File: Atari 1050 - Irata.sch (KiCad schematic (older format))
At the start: 18 parts, among them J1 6507, J2 Conn_01x05, U1 6502, U2 6264, U3 27C64, U4 74LS42, U5 74LS00, U6 74LS00, U7 74LS139, U8 74LS30

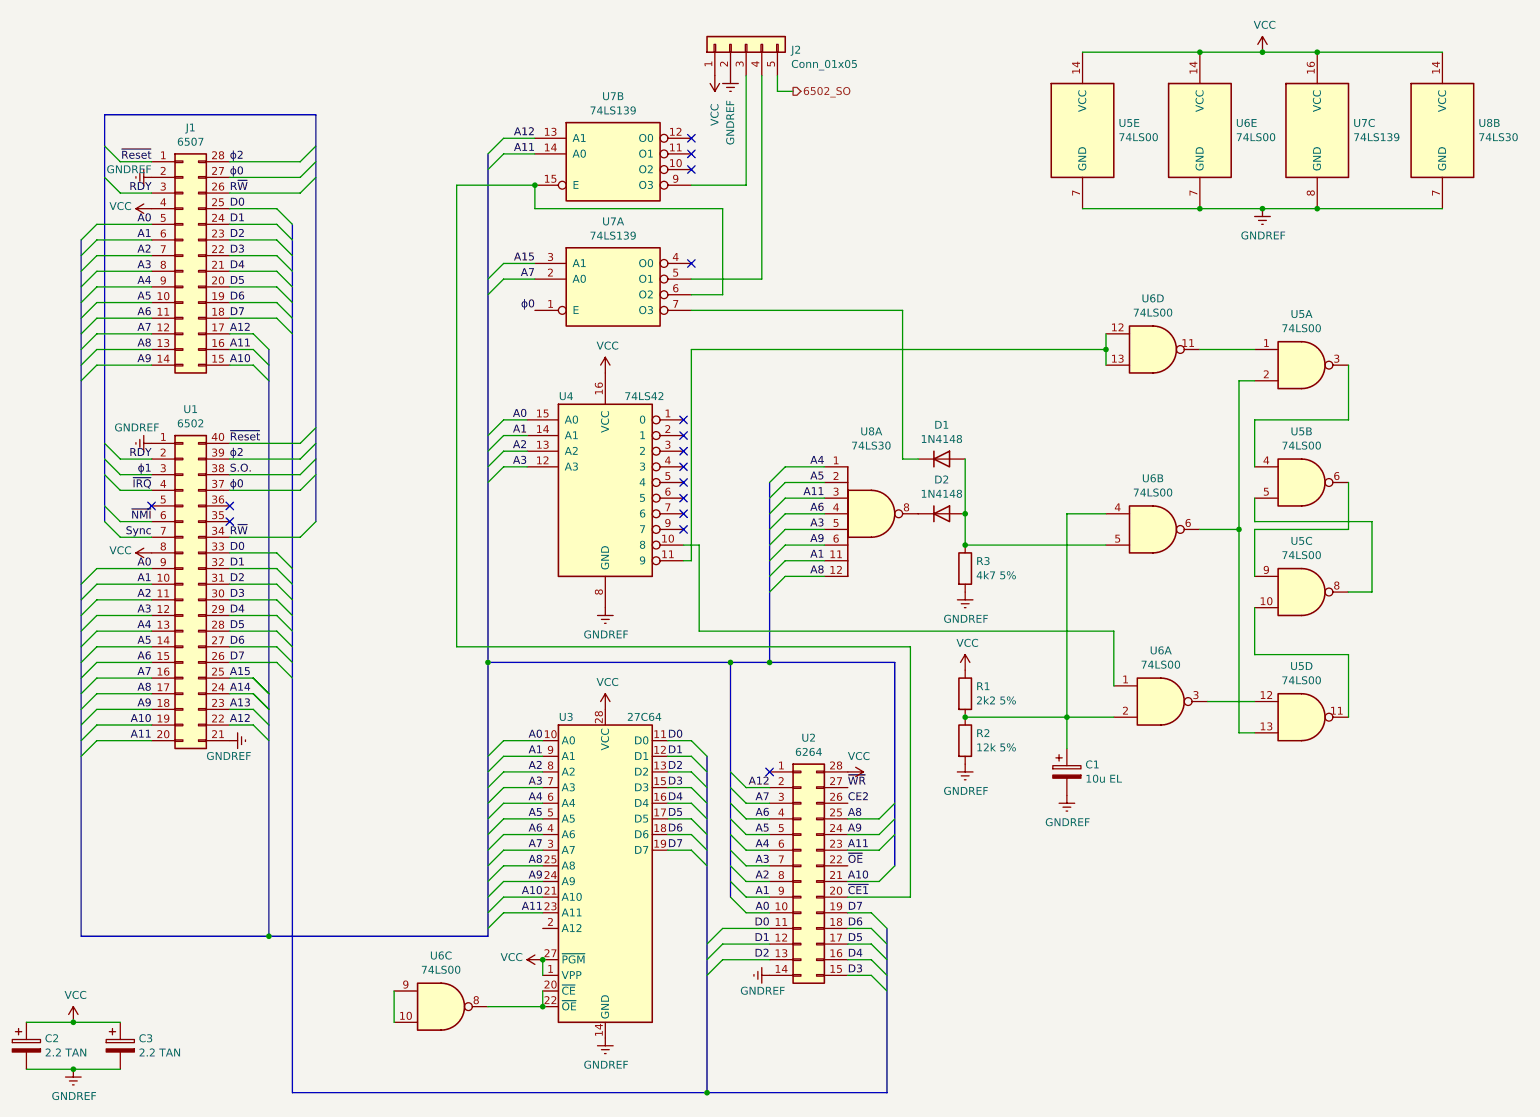
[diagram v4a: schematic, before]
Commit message: Remaining connections, pdf schematics
* Added control bus between existing schematic and J1/U1
* Connected RDY, NMI and INT according to the board layout
* Plotted the schematic at /pdf directory
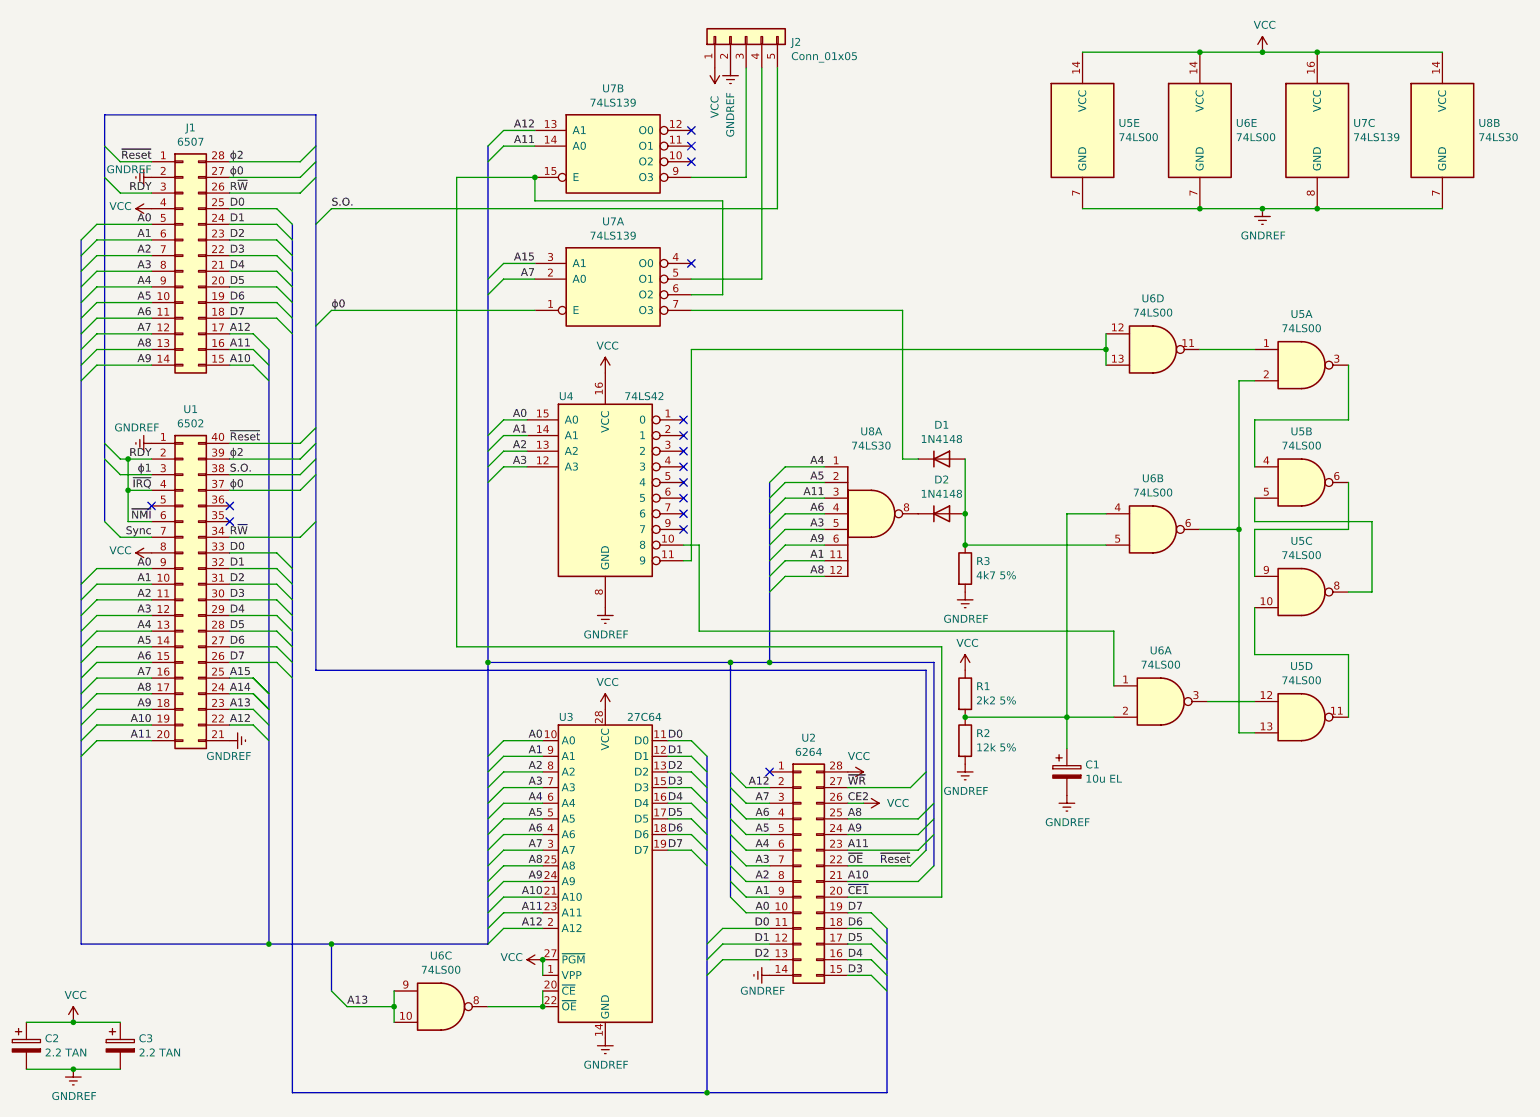
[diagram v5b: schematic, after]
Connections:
- net 6502_SO is gone; now on net S.O.: J2.5 (Pin_5)
- net CE2 is gone; now on net VCC: U2.26 (Pin_26)
- net ~IRQ is gone; now on net RDY: U1.4 (Pin_4)
- net ~NMI is gone; now on net RDY: U1.6 (Pin_6)
- net ~Reset is gone; now on net ~OE: J1.1 (Pin_1), U1.40 (Pin_40)
- net A12: now also U3.2 (A12)
- net A13: now also U6.10, U6.9
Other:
- moved on the sheet: J2, U7B
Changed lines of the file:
@@
 encoding utf-8
 Sheet 1 1
-Title ""
-Date ""
-Rev ""
+Title "Main board"
+Date "2022-03-07"
+Rev "1"
 Comp ""
 Comment1 ""
@@
 	7850 2650 7850 2750
 Wire Wire Line
-	3300 6850 3300 7050
+	3300 6850 3300 6950
 Wire Wire Line
 	8450 2750 8800 2750
@@
 L 74xx:74LS139 U7
 U 2 1 6226DDE8
-P 4700 1500
-F 0 "U7" H 4700 1867 50  0000 C CNN
-F 1 "74LS139" H 4700 1776 50  0000 C CNN
-F 2 "" H 4700 1500 50  0001 C CNN
-F 3 "http://www.ti.com/lit/ds/symlink/sn74ls139a.pdf" H 4700 1500 50  0001 C CNN
-	2    4700 1500
+P 4700 1450
+F 0 "U7" H 4700 1817 50  0000 C CNN
+F 1 "74LS139" H 4700 1726 50  0000 C CNN
+F 2 "" H 4700 1450 50  0001 C CNN
+F 3 "http://www.ti.com/lit/ds/symlink/sn74ls139a.pdf" H 4700 1450 50  0001 C CNN
+	2    4700 1450
 	1    0    0    -1
 $EndComp
@@
 L Connector_Generic:Conn_01x05 J2
 U 1 1 622CA127
-P 5550 800
-F 0 "J2" V 5514 512 50  0000 R CNN
-F 1 "Conn_01x05" V 5423 512 50  0000 R CNN
-F 2 "" H 5550 800 50  0001 C CNN
-F 3 "~" H 5550 800 50  0001 C CNN
-	1    5550 800
+P 5550 750
+F 0 "J2" V 5514 462 50  0000 R CNN
+F 1 "Conn_01x05" V 5423 462 50  0000 R CNN
+F 2 "" H 5550 750 50  0001 C CNN
+F 3 "~" H 5550 750 50  0001 C CNN
+	1    5550 750
 	0    -1   -1   0
 $EndComp
@@
 L power:GNDREF #PWR?
 U 1 1 622CB691
-P 5450 1000
-F 0 "#PWR?" H 5450 750 50  0001 C CNN
-F 1 "GNDREF" V 5450 700 50  0000 C CNN
-F 2 "" H 5450 1000 50  0001 C CNN
-F 3 "" H 5450 1000 50  0001 C CNN
-	1    5450 1000
+P 5450 950
+F 0 "#PWR?" H 5450 700 50  0001 C CNN
+F 1 "GNDREF" V 5450 650 50  0000 C CNN
+F 2 "" H 5450 950 50  0001 C CNN
+F 3 "" H 5450 950 50  0001 C CNN
+	1    5450 950
 	1    0    0    -1
 $EndComp
@@
 L power:VCC #PWR?
 U 1 1 622CCB5A
-P 5350 1000
-F 0 "#PWR?" H 5350 850 50  0001 C CNN
-F 1 "VCC" V 5350 1250 50  0000 C CNN
-F 2 "" H 5350 1000 50  0001 C CNN
-F 3 "" H 5350 1000 50  0001 C CNN
-	1    5350 1000
+P 5350 950
+F 0 "#PWR?" H 5350 800 50  0001 C CNN
+F 1 "VCC" V 5350 1200 50  0000 C CNN
+F 2 "" H 5350 950 50  0001 C CNN
+F 3 "" H 5350 950 50  0001 C CNN
+	1    5350 950
 	1    0    0    1
 $EndComp
 Wire Wire Line
-	5550 1000 5550 1700
-Wire Wire Line
-	5550 1700 5200 1700
-NoConn ~ 5200 1600
-NoConn ~ 5200 1400
-Text HLabel 5850 1100 2    50   Output ~ 0
-6502_SO
-Wire Wire Line
-	5850 1100 5750 1100
-Wire Wire Line
-	5750 1100 5750 1000
+	5550 950  5550 1650
+Wire Wire Line
+	5550 1650 5200 1650
+NoConn ~ 5200 1550
+NoConn ~ 5200 1350
 Text Label 4150 3200 2    50   ~ 0
 A0
@@
 Text Label 5050 5950 0    50   ~ 0
 D7
-Text Label 4200 2500 2    50   ~ 0
+Text Label 2900 2500 0    50   ~ 0
 ϕ0
 Text Label 4200 2300 2    50   ~ 0
@@
 A15
 Wire Wire Line
-	5650 1000 5650 2300
+	5650 950  5650 2300
 Wire Wire Line
 	5650 2300 5200 2300
-Text Label 4200 1500 2    50   ~ 0
+Text Label 4200 1450 2    50   ~ 0
 A11
-Text Label 4200 1400 2    50   ~ 0
+Text Label 4200 1350 2    50   ~ 0
 A12
 $Comp
@@
 $EndComp
 Wire Wire Line
-	6200 6250 6600 6250
-Wire Wire Line
-	6600 6250 6600 4650
-Wire Wire Line
-	6600 4650 3700 4650
-Wire Wire Line
-	3700 4650 3700 1700
-Wire Wire Line
-	3700 1700 4200 1700
-Wire Wire Line
-	5400 2400 5400 1850
-Wire Wire Line
-	5400 1850 4200 1850
-Wire Wire Line
-	4200 1850 4200 1700
+	6200 6250 6800 6250
+Wire Wire Line
+	6800 6250 6800 4650
+Wire Wire Line
+	6800 4650 3700 4650
+Wire Wire Line
+	3700 4650 3700 1650
+Wire Wire Line
+	3700 1650 4200 1650
+Wire Wire Line
+	5400 2400 5400 1800
+Wire Wire Line
+	5400 1800 4200 1800
+Wire Wire Line
+	4200 1800 4200 1650
 Wire Wire Line
 	5200 2400 5400 2400
-Connection ~ 4200 1700
+Connection ~ 4200 1650
 Wire Wire Line
 	5200 2500 6550 2500
@@
 Wire Wire Line
 	6550 3450 6650 3450
-NoConn ~ 5200 1500
+NoConn ~ 5200 1450
 Text Label 6050 3500 2    50   ~ 0
 A4
@@
 A8
 Entry Wire Line
-	3900 1500 4000 1400
-Entry Wire Line
-	3900 1600 4000 1500
+	3900 1450 4000 1350
+Entry Wire Line
+	3900 1550 4000 1450
 Entry Wire Line
 	3900 2300 4000 2200
@@
 	3900 3600 4000 3500
 Wire Wire Line
-	4000 1400 4200 1400
-Wire Wire Line
-	4200 1500 4000 1500
+	4000 1350 4200 1350
+Wire Wire Line
+	4200 1450 4000 1450
 Wire Wire Line
 	4000 2200 4200 2200
@@
 	5450 6250 5550 6350
 Entry Wire Line
-	6400 5750 6500 5650
-Entry Wire Line
-	6400 5850 6500 5750
-Entry Wire Line
-	6400 5950 6500 5850
-Entry Wire Line
-	6400 6150 6500 6050
+	6650 5750 6750 5650
+Entry Wire Line
+	6650 5850 6750 5750
+Entry Wire Line
+	6650 5950 6750 5850
+Entry Wire Line
+	6650 6150 6750 6050
 Wire Wire Line
 	5550 5550 5700 5550
@@
 	5550 6350 5700 6350
 Wire Wire Line
-	6400 6150 6200 6150
-Wire Wire Line
-	6200 5950 6400 5950
-Wire Wire Line
-	6400 5850 6200 5850
-Wire Wire Line
-	6200 5750 6400 5750
+	6650 6150 6200 6150
+Wire Wire Line
+	6200 5950 6650 5950
+Wire Wire Line
+	6650 5850 6200 5850
+Wire Wire Line
+	6200 5750 6650 5750
 Connection ~ 5450 4750
 Wire Bus Line
 	5450 4750 3900 4750
 Wire Bus Line
-	5700 4750 6500 4750
+	5700 4750 6750 4750
 Connection ~ 5700 4750
 $Comp
@@
 	2400 4850 2500 4950
 Wire Bus Line
-	1300 6500 2500 6500
-Connection ~ 2500 6500
-Wire Bus Line
-	2500 6500 3900 6500
+	1300 6550 2500 6550
+Wire Bus Line
+	2500 6550 2900 6550
 Entry Wire Line
 	2550 4050 2650 4150
@@
 	1450 3850 1550 3950
 Entry Wire Line
-	1450 3750 1550 3850
-Entry Wire Line
-	1450 3550 1550 3650
-Entry Wire Line
 	1450 3450 1550 3550
 Entry Wire Line
 	1450 3350 1550 3450
 Wire Wire Line
-	1550 3450 1750 3450
+	1550 3450 1600 3450
 Wire Wire Line
 	1750 3550 1550 3550
 Wire Wire Line
-	1550 3650 1750 3650
-Wire Wire Line
-	1750 3850 1550 3850
+	1750 3850 1600 3850
 Wire Wire Line
 	1550 3950 1750 3950
@@
 Wire Wire Line
 	950  7350 1250 7350
-Wire Bus Line
-	6500 4750 6500 6050
+$Comp
+L power:VCC #PWR?
+U 1 1 62ED2270
+P 6300 5650
+F 0 "#PWR?" H 6300 5500 50  0001 C CNN
+F 1 "VCC" V 6300 5800 50  0000 L CNN
+F 2 "" H 6300 5650 50  0001 C CNN
+F 3 "" H 6300 5650 50  0001 C CNN
+	1    6300 5650
+	0    1    1    0
+$EndComp
+Wire Wire Line
+	6300 5650 6200 5650
+Text Label 4250 6450 2    50   ~ 0
+A12
+Entry Wire Line
+	3900 6550 4000 6450
+Wire Wire Line
+	4000 6450 4250 6450
+Connection ~ 2500 6550
+Entry Wire Line
+	2900 6850 3000 6950
+Text Label 3000 6950 0    50   ~ 0
+A13
+Wire Wire Line
+	3000 6950 3300 6950
+Connection ~ 3300 6950
+Wire Wire Line
+	3300 6950 3300 7050
+Wire Bus Line
+	2900 6850 2900 6550
+Connection ~ 2900 6550
+Wire Bus Line
+	2900 6550 3900 6550
+Text Label 6600 6050 2    50   ~ 0
+~Reset
+Entry Wire Line
+	6600 6050 6700 5950
+Wire Wire Line
+	6200 6050 6600 6050
+Entry Wire Line
+	6600 5550 6700 5450
+Wire Wire Line
+	6200 5550 6600 5550
+Wire Bus Line
+	6700 4800 2800 4800
+Wire Wire Line
+	1600 3850 1600 3650
+Connection ~ 1600 3650
+Wire Wire Line
+	1600 3650 1750 3650
+Wire Wire Line
+	1600 3650 1600 3450
+Connection ~ 1600 3450
+Wire Wire Line
+	1600 3450 1750 3450
+Entry Wire Line
+	2800 2600 2900 2500
+Wire Wire Line
+	4200 2500 2900 2500
+Entry Wire Line
+	2800 1950 2900 1850
+Wire Wire Line
+	5750 1850 2900 1850
+Wire Wire Line
+	5750 950  5750 1850
+Wire Bus Line
+	6700 4800 6700 5950
+Wire Bus Line
+	6750 4750 6750 6050
 Wire Bus Line
 	6450 6450 6450 7500
 Wire Bus Line
-	2500 2750 2500 6500
+	2500 2750 2500 6550
 Wire Bus Line
 	1450 1250 1450 3850
 Wire Bus Line
-	2800 1250 2800 3850
-Wire Bus Line
 	5450 4750 5450 6250
 Wire Bus Line
 	5700 3600 5700 4750
 Wire Bus Line
-	3900 1500 3900 4750
-Wire Bus Line
-	3900 4750 3900 6500
+	3900 1450 3900 4750
+Wire Bus Line
+	3900 4750 3900 6550
 Wire Bus Line
 	5300 5350 5300 7500
 Wire Bus Line
+	2800 1250 2800 4800
+Wire Bus Line
 	2650 1950 2650 7500
 Wire Bus Line
-	1300 2050 1300 6500
+	1300 2050 1300 6550
+Text Label 2900 1850 0    50   ~ 0
+S.O.
 $EndSCHEMATC
